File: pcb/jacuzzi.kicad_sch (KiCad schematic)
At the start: 78 parts, among them J1 Conn_01x03, J10 Conn_01x02, J2 Conn_01x03, J3 Conn_01x03, J4 Conn_01x04, J5 Conn_01x03, J6 Conn_01x03, J7 Conn_01x02, J8 Conn_01x08, J9 USB_C_Receptacle_PowerOnly_6P, K1 G5LE-1, Q1 MMBT3904, Q2 MMBT3904, Q3 MMBT3904, Q4 IRF4905STRLPBF, Q5 MMBT3904, Q6 IRF4905STRLPBF, U1 LM2575-3.3BU, U2 LM2575-5.0BU, U3 ESP32-DEVKITC-32U

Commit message: some things with jon
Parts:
- removed D22: 20V, Diode_SMD:D_SOD-323, symbol Device:D_Zener
- removed R25: 330, Resistor_SMD:R_0805_2012Metric, symbol Device:R
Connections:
- net +5V: now also R2.1; no longer C1.1, J9.A9 (VBUS), J9.B9 (VBUS)
- net GND: now also Q3.2 (E)
- net VS: now also C1.1, J9.A9 (VBUS), J9.B9 (VBUS); no longer R2.1
- net at R23.1: now also J9.A5 (CC1); no longer J9.B5 (CC2)
- net at R24.1: now also J9.B5 (CC2); no longer J9.A5 (CC1)
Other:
- moved on the sheet: C1, D2, R23, R24, R3

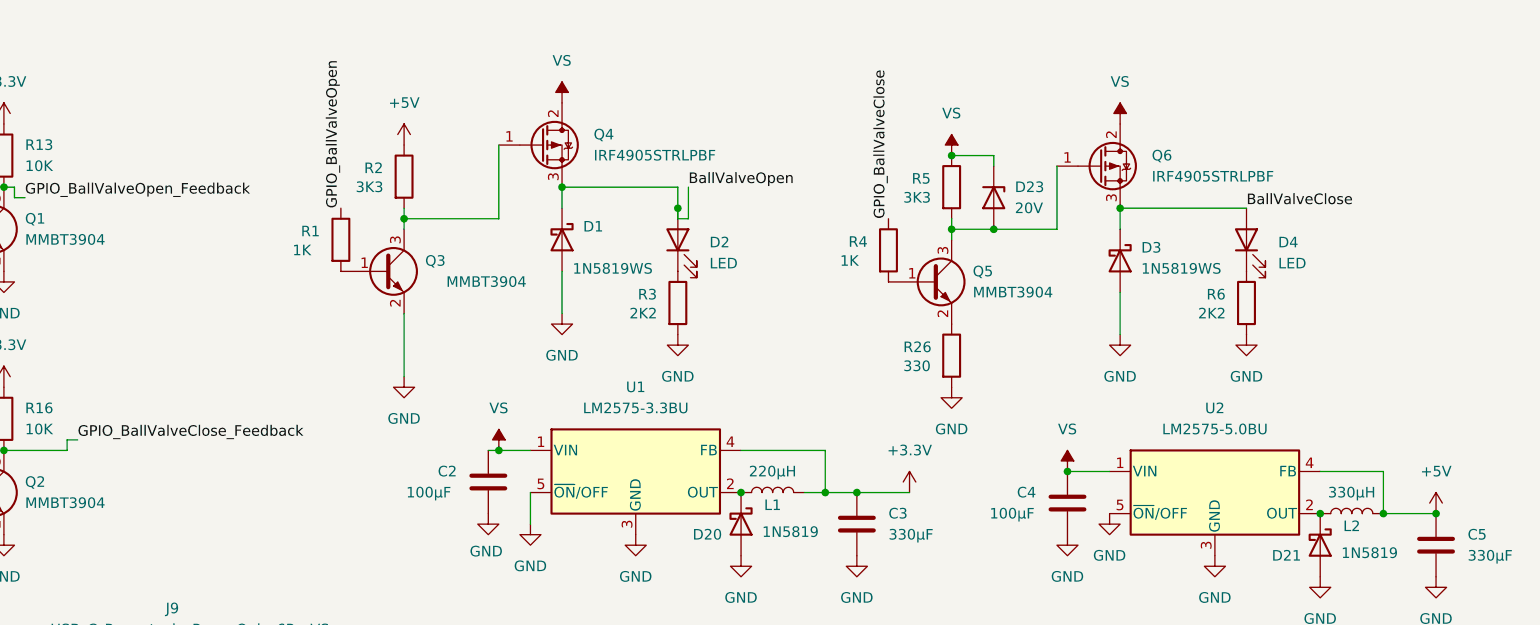
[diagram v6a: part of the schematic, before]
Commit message: working on fixing 5V and voltage supply
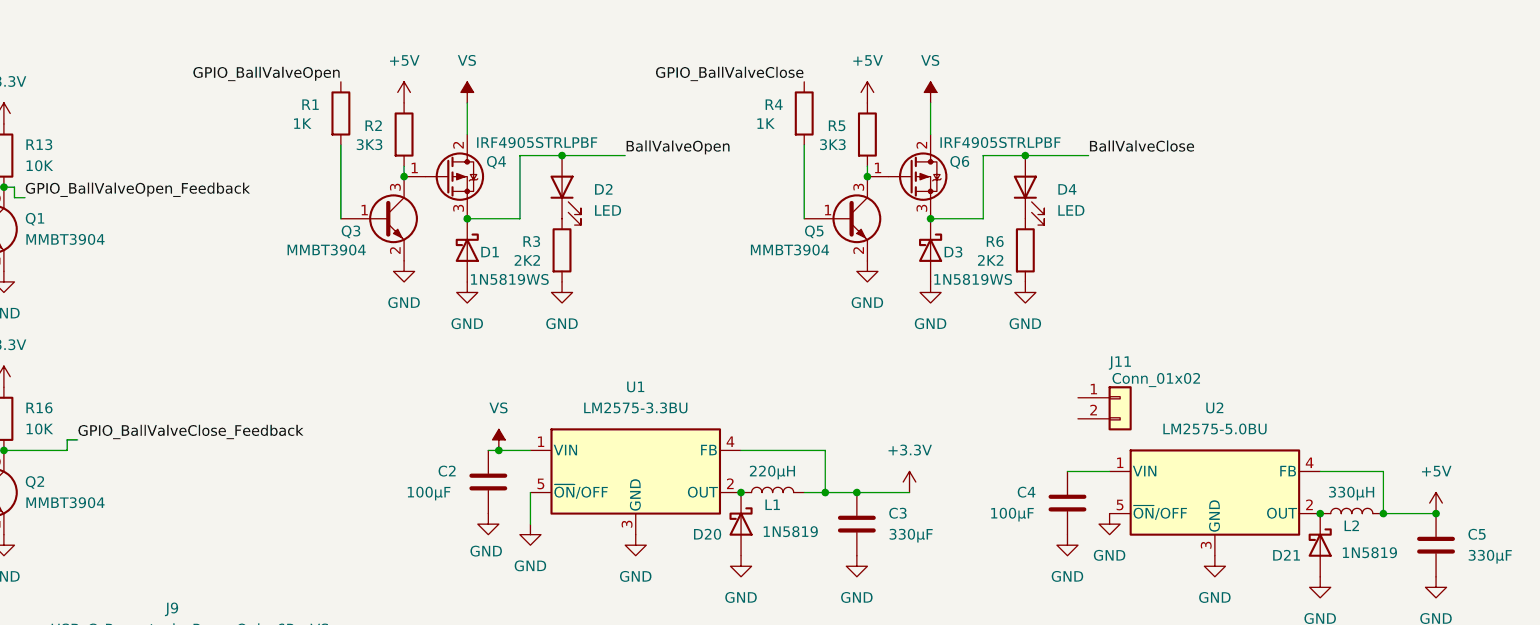
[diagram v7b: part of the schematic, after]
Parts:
- removed D23: 20V, Diode_SMD:D_SOD-323, symbol Device:D_Zener
- removed R26: 330, Resistor_SMD:R_0805_2012Metric, symbol Device:R
- added J11: Conn_01x02, symbol Connector_Generic:Conn_01x02
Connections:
- net +5V: now also R5.1
- net GND: now also Q5.2 (E)
- net VS: no longer C4.1, R5.1, U2.1 (VIN)
- new net: C4.1, U2.1 (VIN)
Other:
- moved on the sheet: D1, Q3, Q4, R1, R2, R3

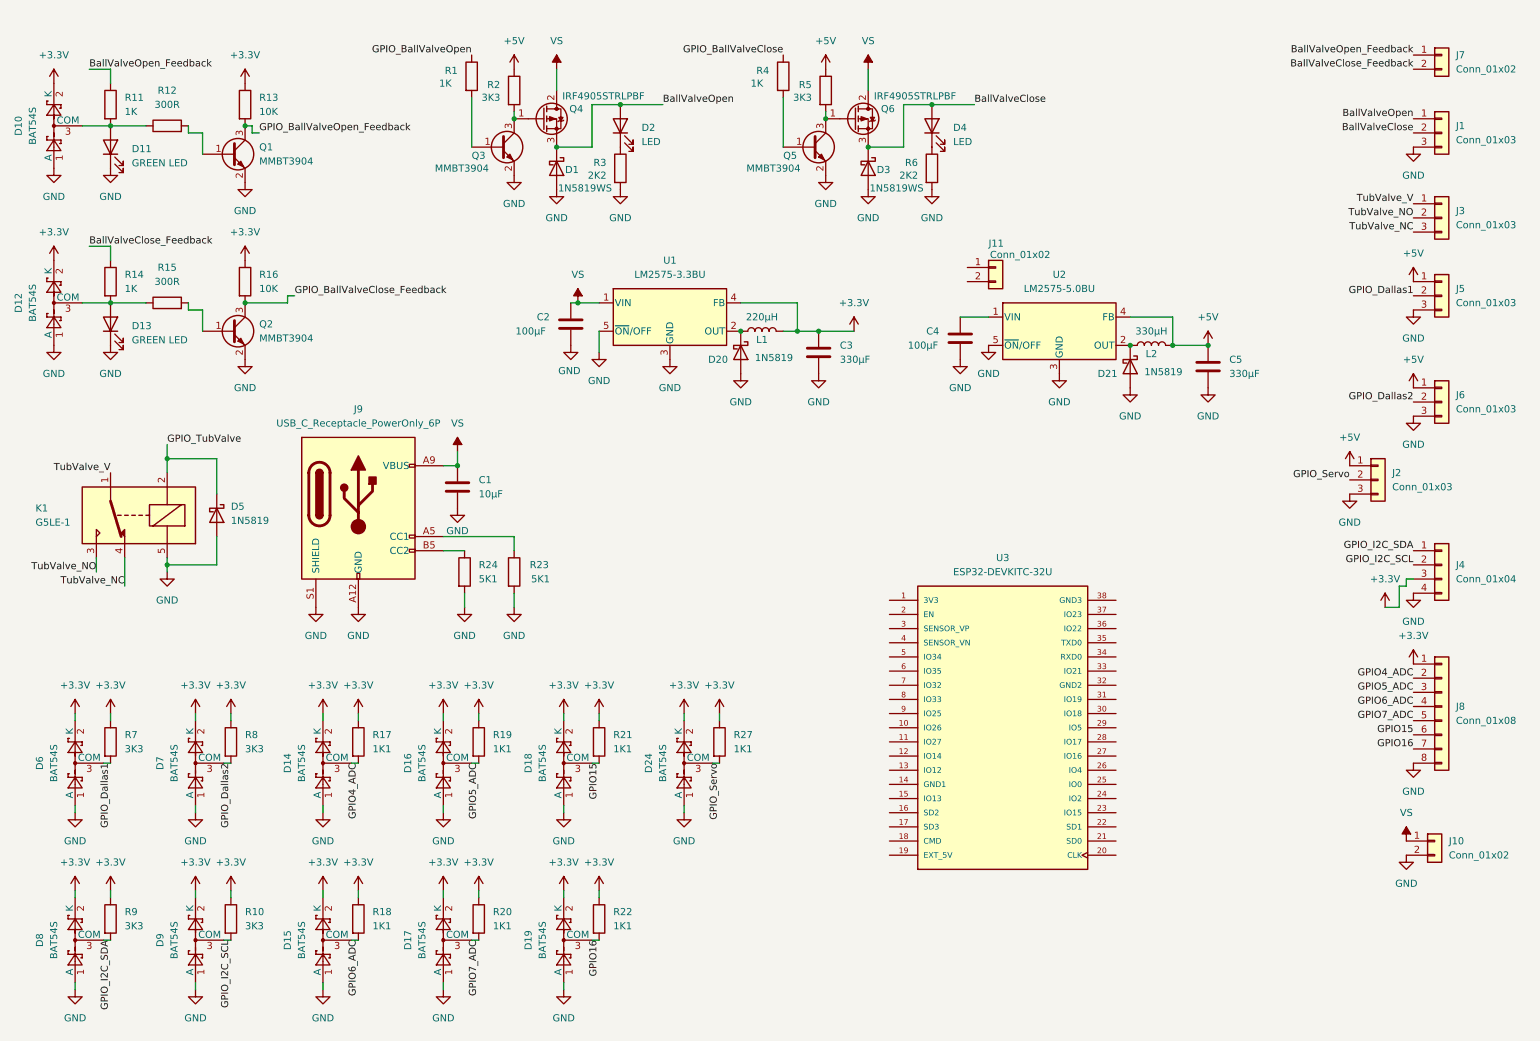
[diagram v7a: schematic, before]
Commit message: schematic is now testable and should be layed out
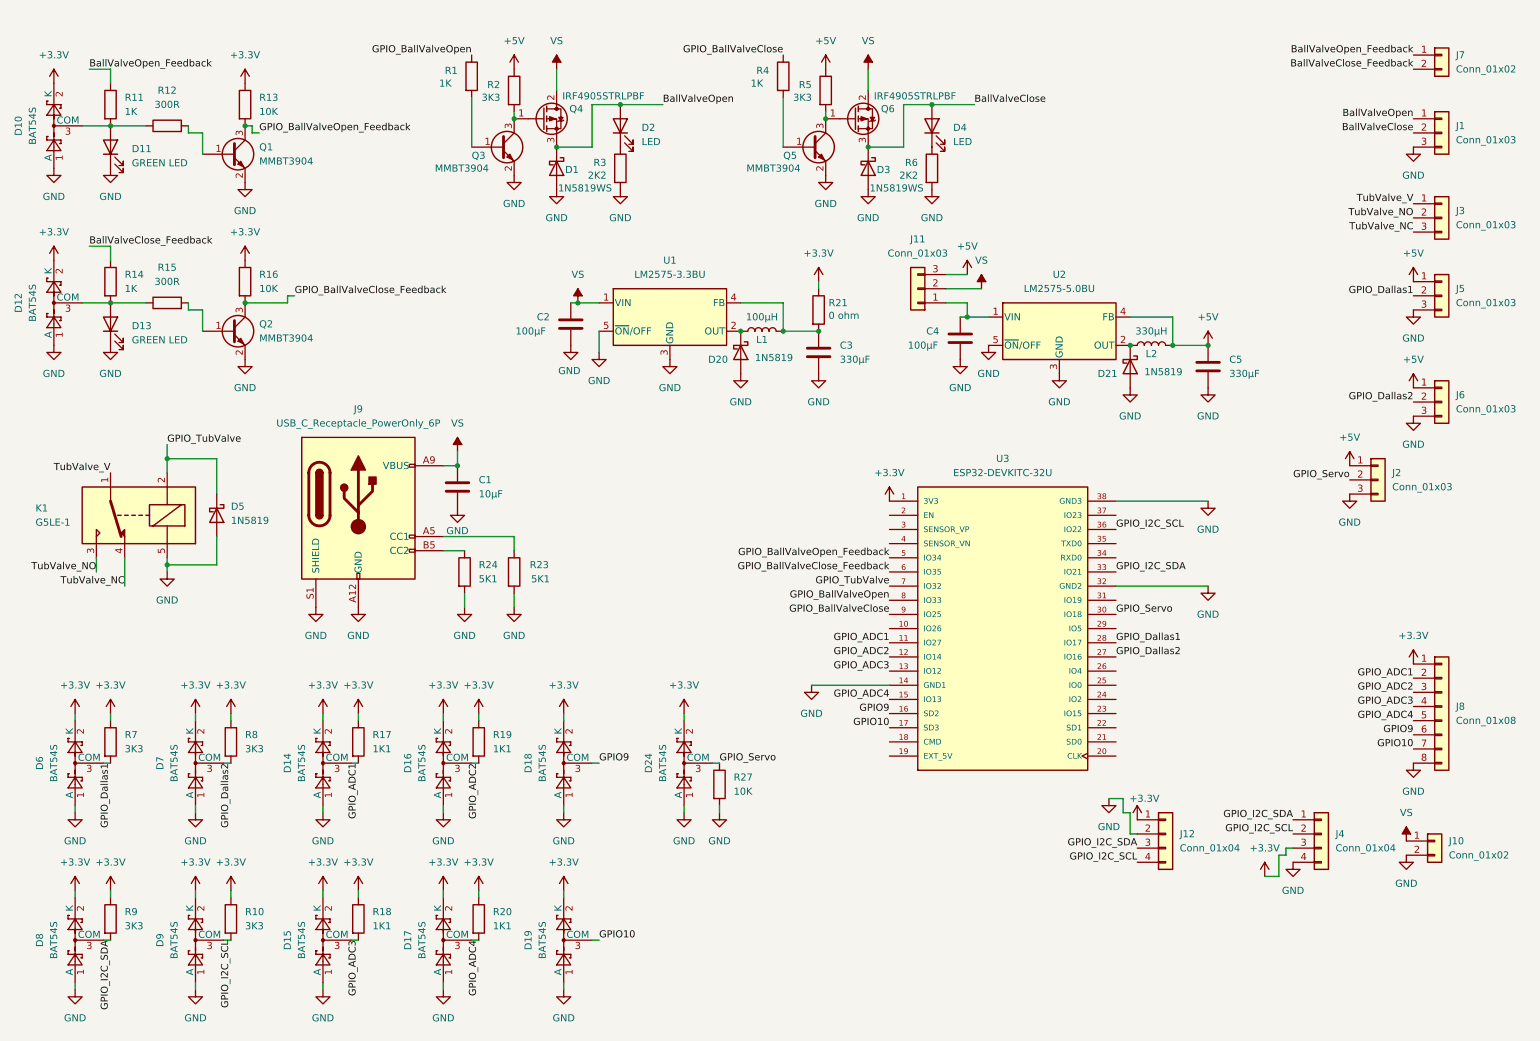
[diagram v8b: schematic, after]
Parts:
- removed J11: Conn_01x02, symbol Connector_Generic:Conn_01x02
- removed R22: 1K1, Resistor_SMD:R_0805_2012Metric, symbol Device:R
- added J11: Conn_01x03, Connector_PinHeader_2.54mm:PinHeader_1x03_P2.54mm_Vertical_SMD_Pin1Left, symbol Connector_Generic:Conn_01x03
- added J12: Conn_01x04, Connector_PinHeader_2.54mm:PinHeader_1x04_P2.54mm_Vertical_SMD_Pin1Left, symbol Connector_Generic:Conn_01x04
- J4: footprint Connector_PinHeader_2.54mm:PinHeader_1x04_P2.54mm_Vertical -> Connector_PinSocket_2.54mm:PinSocket_1x04_P2.54mm_Vertical_SMD_Pin1Left
- J8: footprint Connector_PinHeader_2.54mm:PinHeader_1x08_P2.54mm_Vertical -> Connector_PinHeader_2.54mm:PinHeader_1x08_P2.54mm_Vertical_SMD_Pin1Left
- L1: value 220µH -> 100µH
- R21: value 1K1 -> 0 ohm
- R27: value 1K1 -> 10K
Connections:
- net GPIO16 is gone; now on net GPIO10: D19.3 (COM), J8.7 (Pin_7)
- net GPIO4_ADC is gone; now on net GPIO_ADC1: D14.3 (COM), J8.2 (Pin_2), R17.2
- net GPIO5_ADC is gone; now on net GPIO_ADC2: D16.3 (COM), J8.3 (Pin_3), R19.2
- net GPIO6_ADC is gone; now on net GPIO_ADC3: D15.3 (COM), J8.4 (Pin_4), R18.2
- net GPIO7_ADC is gone; now on net GPIO_ADC4: D17.3 (COM), J8.5 (Pin_5), R20.2
- net +3.3V: now also U3.1 (3V3), J12.1 (Pin_1); no longer C3.1, L1.2, R27.1, U1.4 (FB)
- net +5V: now also J11.3 (Pin_3)
- net GND: now also R27.2, U3.14 (GND1), U3.32 (GND2), U3.38 (GND3), J12.2 (Pin_2)
- net GPIO_BallValveClose: now also U3.9 (IO25)
- net GPIO_BallValveClose_Feedback: now also U3.6 (IO35)
- net GPIO_BallValveOpen: now also U3.8 (IO33)
- net GPIO_BallValveOpen_Feedback: now also U3.5 (IO34)
- net GPIO_Dallas1: now also U3.28 (IO17)
- net GPIO_Dallas2: now also U3.27 (IO16)
- net GPIO_I2C_SCL: now also U3.36 (IO22), J12.4 (Pin_4)
- net GPIO_I2C_SDA: now also U3.33 (IO21), J12.3 (Pin_3)
- net GPIO_Servo: now also R27.1, U3.30 (IO18); no longer R27.2
- net GPIO_TubValve: now also U3.7 (IO32)
- net VS: now also J11.2 (Pin_2)
- net at C4.1, U2.1 (VIN): now also J11.1 (Pin_1)
- net GPIO_ADC1: now reaches U3.11 (IO27)
- net GPIO_ADC2: now reaches U3.12 (IO14)
- net GPIO_ADC3: now reaches U3.13 (IO12)
- net GPIO_ADC4: now reaches U3.15 (IO13)
- net GPIO9: now reaches U3.16 (SD2)
- net GPIO9: now also D18.3 (COM), J8.6 (Pin_6)
- net GPIO10: now reaches U3.17 (SD3)
- removed net GPIO15: D18.3 (COM), J8.6 (Pin_6), R21.2
- new net: C3.1, L1.2, R21.2, U1.4 (FB)
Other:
- moved on the sheet: J4, R27, U3
